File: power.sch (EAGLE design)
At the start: 65 parts, among them J1 POWER_JACKPTH_BREAD, T1 SINGLE_NCHAN_FET, T2 SINGLE_NCHAN_FET, T3 SINGLE_NCHAN_FET, U1 MOSFET_PCHAN_20A, U14 MOSFET_PCHAN_20A, U2 MOSFET_PCHAN_20A

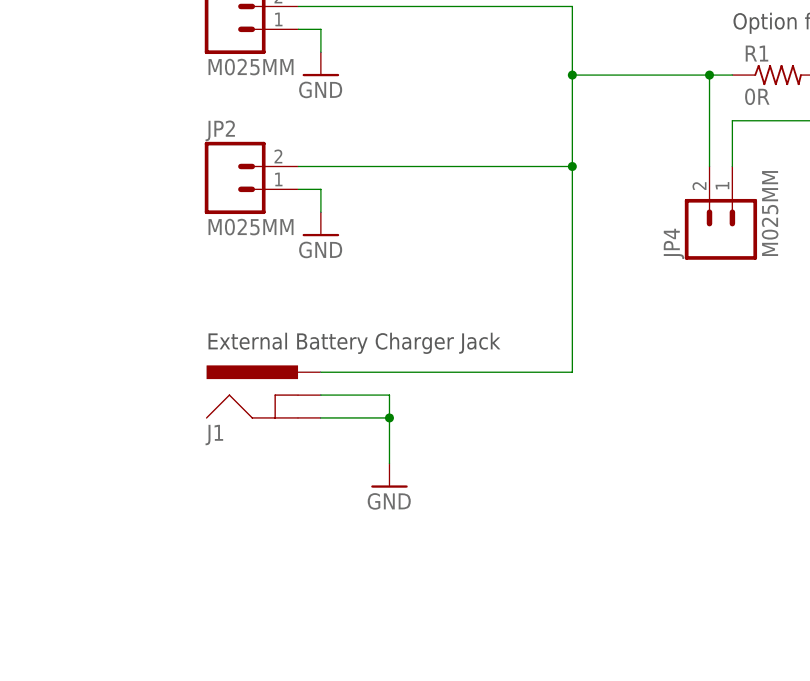
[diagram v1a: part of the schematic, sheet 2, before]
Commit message: Switching to teensy for flight computer
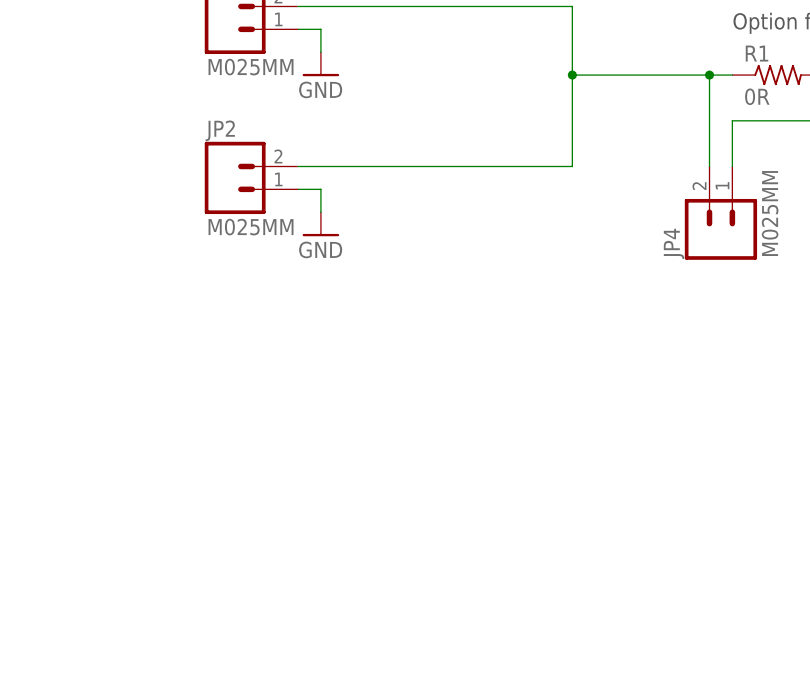
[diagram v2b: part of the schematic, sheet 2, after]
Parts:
- removed J1: POWER_JACKPTH_BREAD, SparkFun-Connectors:POWER_JACKPTH_BREAD
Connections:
- net BATT_INPUT: no longer J1.PWR
- net GND: no longer J1.GND, J1.GNDBREAK
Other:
- note removed: "External Battery Charger Jack"
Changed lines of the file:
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@@
 <part name="U$11" library="Widetronix" deviceset="BETABATTERY" device=""/>
 <part name="U$12" library="Widetronix" deviceset="BETABATTERY" device=""/>
-<part name="J1" library="SparkFun-Connectors" deviceset="POWER_JACK" device="PTH_BREAD"/>
 <part name="GND2" library="SparkFun-Aesthetics" deviceset="GND" device=""/>
-<part name="GND3" library="SparkFun-Aesthetics" deviceset="GND" device=""/>
 <part name="JP1" library="SparkFun-Connectors" deviceset="M02" device="5MM"/>
 <part name="JP2" library="SparkFun-Connectors" deviceset="M02" device="5MM"/>
@@
 <text x="22.86" y="177.8" size="1.778" layer="97">CubeSat Bus Connectors</text>
 <text x="-15.24" y="76.2" size="1.778" layer="97">Battery Terminals</text>
-<text x="-12.7" y="30.48" size="1.778" layer="97">External Battery Charger Jack</text>
 <text x="33.02" y="-25.4" size="1.778" layer="97">Burn Wire 3 Terminal</text>
 </plain>
@@
 <instance part="U$5" gate="G$1" x="-111.76" y="124.46" rot="R90"/>
 <instance part="U$6" gate="G$1" x="-111.76" y="88.9" rot="R90"/>
-<instance part="J1" gate="G$1" x="-2.54" y="20.32" smashed="yes">
-<attribute name="NAME" x="-12.7" y="20.32" size="1.778" layer="95"/>
-</instance>
-<instance part="GND3" gate="1" x="7.62" y="15.24"/>
 <instance part="JP1" gate="G$1" x="-10.16" y="66.04"/>
 <instance part="JP2" gate="G$1" x="-10.16" y="48.26"/>
@@
 <net name="GND" class="0">
 <segment>
-<pinref part="J1" gate="G$1" pin="GND"/>
-<wire x1="0" y1="22.86" x2="7.62" y2="22.86" width="0.1524" layer="91"/>
-<pinref part="J1" gate="G$1" pin="GNDBREAK"/>
-<wire x1="0" y1="25.4" x2="7.62" y2="25.4" width="0.1524" layer="91"/>
-<wire x1="7.62" y1="25.4" x2="7.62" y2="22.86" width="0.1524" layer="91"/>
-<wire x1="7.62" y1="22.86" x2="7.62" y2="17.78" width="0.1524" layer="91"/>
-<pinref part="GND3" gate="1" pin="GND"/>
-<junction x="7.62" y="22.86"/>
-</segment>
-<segment>
 <pinref part="JP1" gate="G$1" pin="1"/>
 <wire x1="-2.54" y1="66.04" x2="0" y2="66.04" width="0.1524" layer="91"/>
@@
 <net name="BATT_INPUT" class="0">
 <segment>
-<pinref part="J1" gate="G$1" pin="PWR"/>
 <pinref part="JP2" gate="G$1" pin="2"/>
 <pinref part="JP1" gate="G$1" pin="2"/>
@@
 <wire x1="-2.54" y1="50.8" x2="27.94" y2="50.8" width="0.1524" layer="91"/>
 <wire x1="27.94" y1="50.8" x2="27.94" y2="60.96" width="0.1524" layer="91"/>
-<wire x1="0" y1="27.94" x2="27.94" y2="27.94" width="0.1524" layer="91"/>
-<wire x1="27.94" y1="27.94" x2="27.94" y2="50.8" width="0.1524" layer="91"/>
-<junction x="27.94" y="50.8"/>
 <junction x="27.94" y="60.96"/>
 </segment>
